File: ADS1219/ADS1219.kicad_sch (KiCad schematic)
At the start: 3 parts

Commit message: Sync
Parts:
- added C1, C2: 0.1μf, Capacitor_SMD:C_0805_2012Metric_Pad1.18x1.45mm_HandSolder, symbol Device:C
- added JP1, JP2, JP3, JP4, JP5, JP6, JP7, JP8: SolderJumper_2_Open, Jumper:SolderJumper-2_P1.3mm_Open_TrianglePad1.0x1.5mm, symbol Jumper:SolderJumper_2_Open
- added R1, R2, R3: 4.7k, Resistor_SMD:R_0805_2012Metric_Pad1.20x1.40mm_HandSolder, symbol Device:R
- J1: renamed from J?; footprint Connector_PinHeader_1.00mm:PinHeader_1x04_P1.00mm_Vertical -> Connector_JST:JST_SH_BM04B-SRSS-TB_1x04-1MP_P1.00mm_Vertical
- J2: renamed from J?; footprint Connector_PinHeader_1.00mm:PinHeader_1x06_P1.00mm_Vertical -> Connector_PinHeader_2.54mm:PinHeader_1x06_P2.54mm_Vertical
- gave numbers to parts that had none: 1
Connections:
- net +3V3: now also U1.12 (AVDD), U1.13 (DVDD), U1.3 (RESET_N), C1.2, C2.1, JP2.2 (B), JP6.2 (B), R1.1, R2.1, R3.1
- net AIN0: now also U1.11 (AIN0)
- net AIN1: now also U1.10 (AIN1)
- net AIN2: now also U1.7 (AIN2)
- net AIN3: now also U1.6 (AIN3)
- net GND: now also U1.4 (DGND), U1.5 (AVSS), C1.1, C2.2, JP1.2 (B), JP5.2 (B)
- net SCL: now also U1.16 (SCL), JP4.2 (B), JP8.2 (B), R3.2
- net SDA: now also U1.15 (SDA), JP3.2 (B), JP7.2 (B), R1.2
- net A0: now reaches U1.1 (A0)
- net A0: now also JP5.1 (A), JP6.1 (A), JP7.1 (A), JP8.1 (A)
- net at U1.14 (DRDY_N): now also R2.2
- net A1: now reaches U1.2 (A1)
- net A1: now also JP1.1 (A), JP2.1 (A), JP3.1 (A), JP4.1 (A)
- no-connect marks 0 -> 2

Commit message: futher revisions
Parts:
- added H1, H2: MountingHole, MountingHole:MountingHole_2.5mm, symbol Mechanical:MountingHole
- J1: footprint Connector_JST:JST_SH_BM04B-SRSS-TB_1x04-1MP_P1.00mm_Vertical -> Connector_JST:JST_SH_SM04B-SRSS-TB_1x04-1MP_P1.00mm_Horizontal
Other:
- company: (none) -> BecauseImclever.com
- moved on the sheet: C1, C2, J1, J2, JP1, JP2, JP3, JP4, JP5, JP6, JP7, JP8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

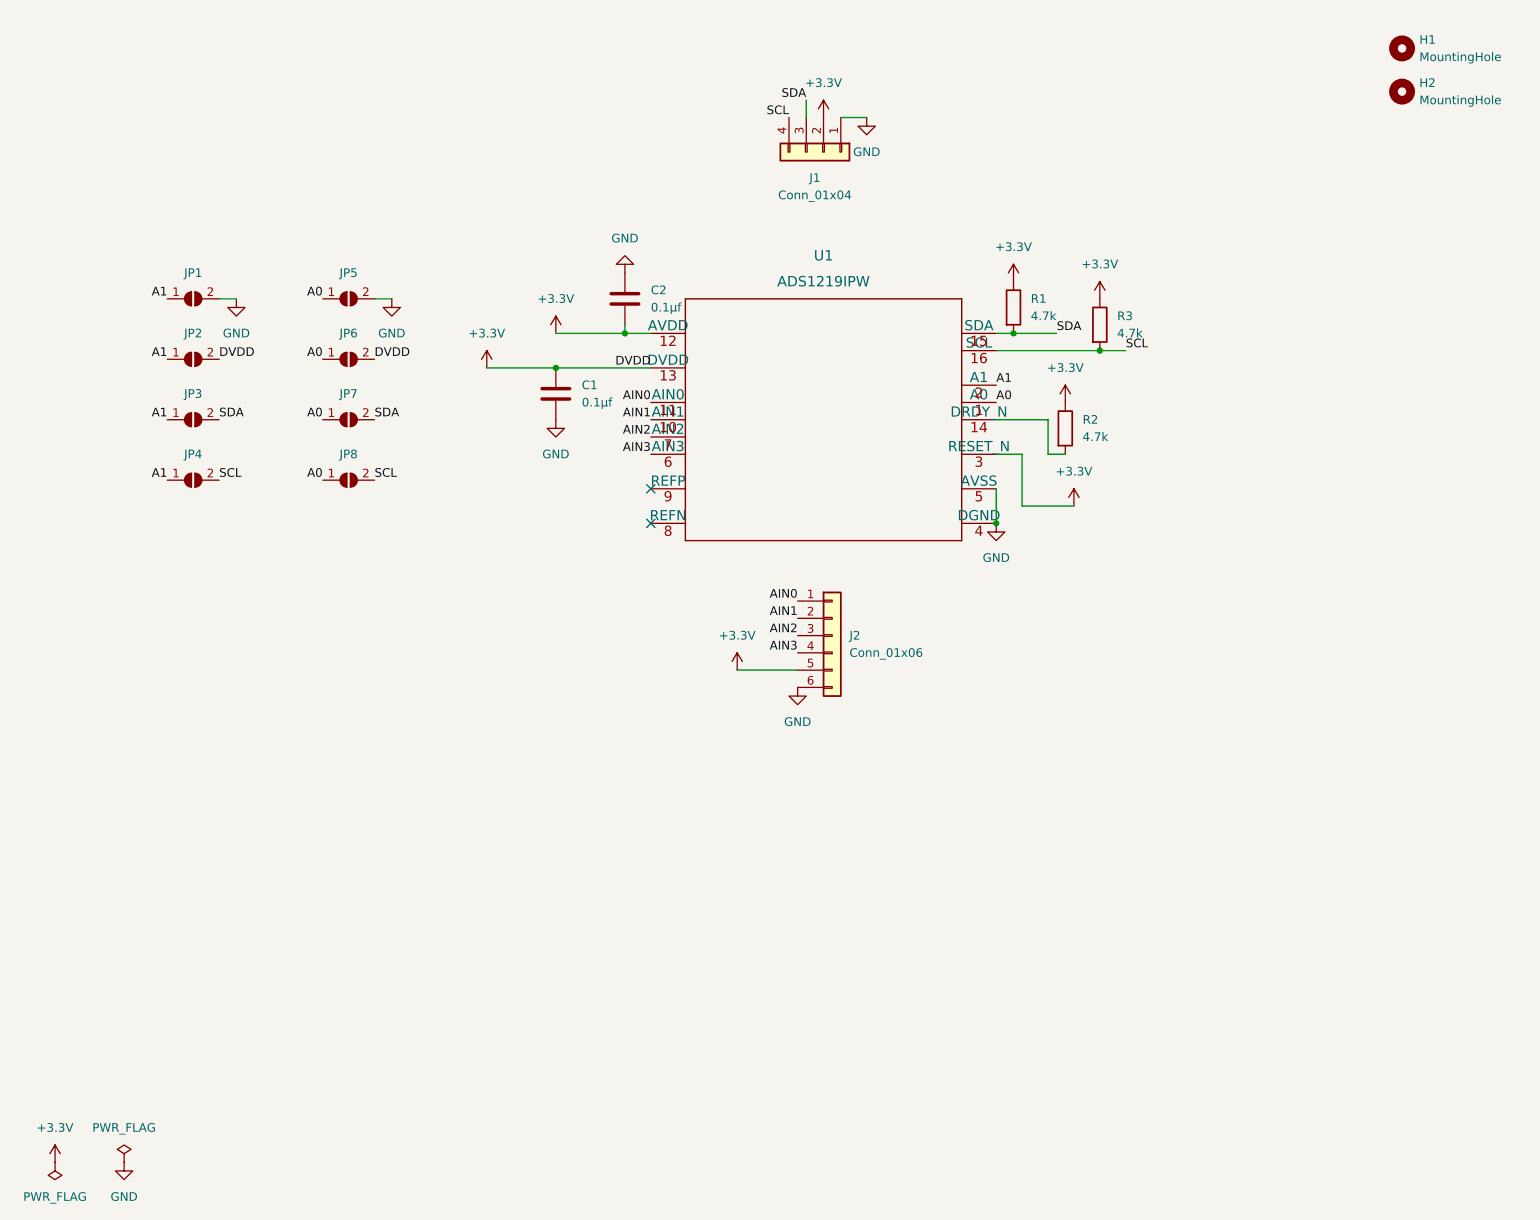
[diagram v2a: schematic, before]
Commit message: ADC nearly complete
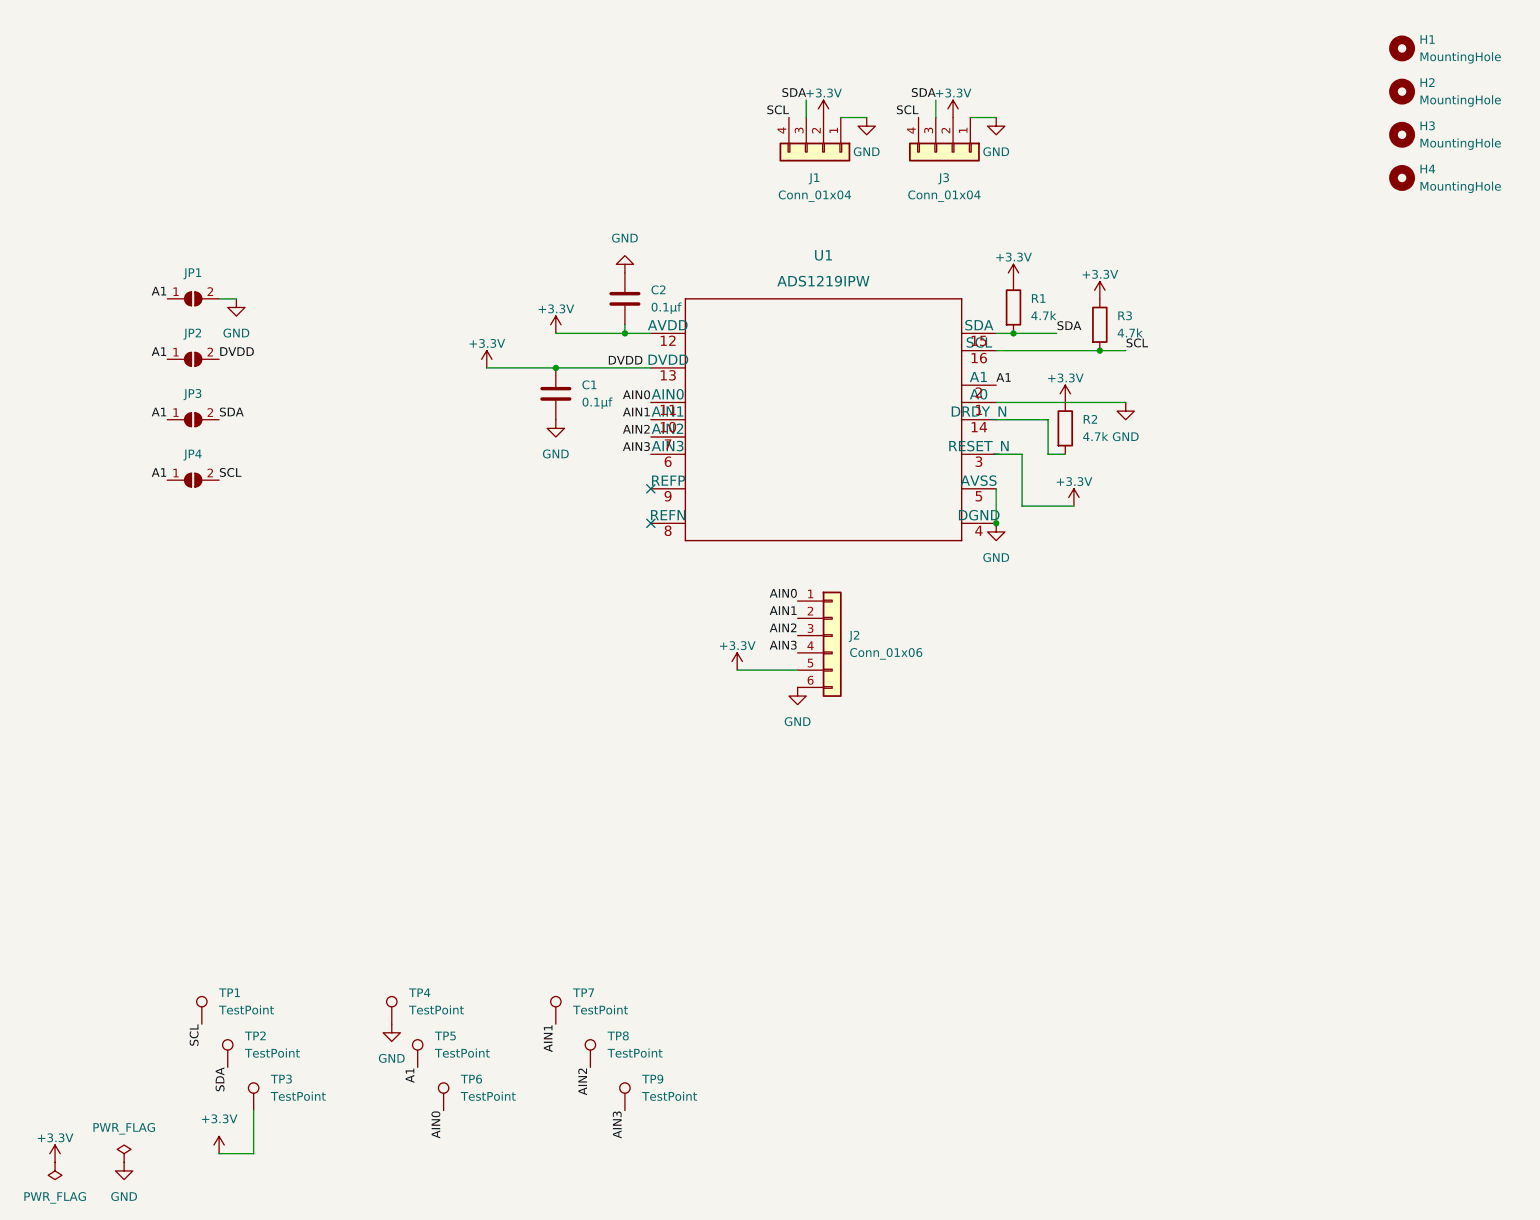
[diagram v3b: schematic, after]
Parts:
- removed JP5, JP6, JP7, JP8: SolderJumper_2_Open, Jumper:SolderJumper-2_P1.3mm_Open_TrianglePad1.0x1.5mm, symbol Jumper:SolderJumper_2_Open
- added H3, H4: MountingHole, MountingHole:MountingHole_2.5mm, symbol Mechanical:MountingHole
- added J3: Conn_01x04, Connector_JST:JST_SH_SM04B-SRSS-TB_1x04-1MP_P1.00mm_Horizontal, symbol Connector_Generic:Conn_01x04
- added TP1, TP2, TP3, TP4, TP5, TP6, TP7, TP8, TP9: TestPoint, TestPoint:TestPoint_Pad_1.0x1.0mm, symbol Connector:TestPoint
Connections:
- net A0 is gone; now on net GND: U1.1 (A0)
- net A1: now also TP5.1
- net AIN0: now also TP6.1
- net AIN1: now also TP7.1
- net AIN2: now also TP8.1
- net AIN3: now also TP9.1
- net GND: now also J3.1 (Pin_1), TP4.1
- net SCL: now also J3.4 (Pin_4), TP1.1
- net SDA: now also J3.3 (Pin_3), TP2.1
- net +3V3 renamed +3.3V
- net +3.3V: now also J3.2 (Pin_2), TP3.1

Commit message: Updating the adc board with a vref
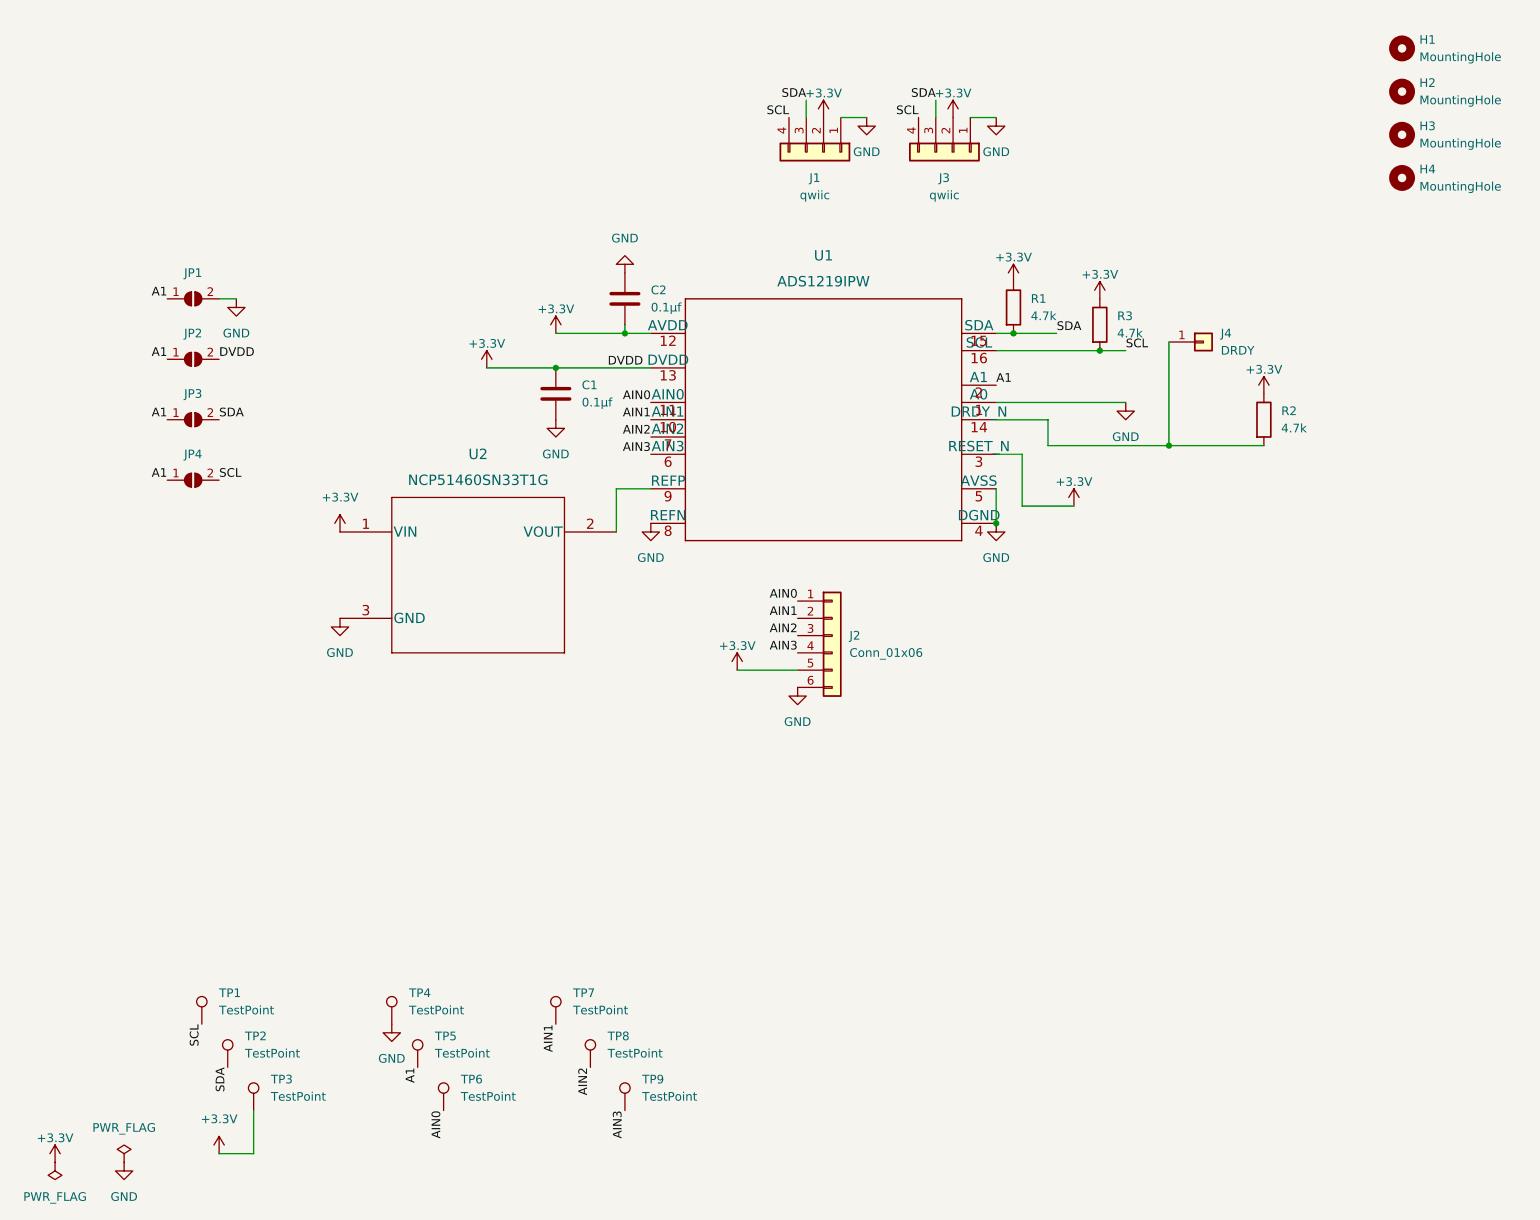
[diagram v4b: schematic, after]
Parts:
- added J4: DRDY, symbol Connector_Generic:Conn_01x01
- added U2: NCP51460SN33T1G, NCP51460SN33T1G:NCP51460SN33T1G, symbol NCP51460SN33T1G:NCP51460SN33T1G
- J1, J3: value Conn_01x04 -> qwiic
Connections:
- net +3.3V: now also U2.1 (VIN)
- net GND: now also U1.8 (REFN), U2.3 (GND)
- net at R2.2, U1.14 (DRDY_N): now also J4.1 (Pin_1)
- net at U1.9 (REFP): now also U2.2 (VOUT)
- no-connect marks 2 -> 0
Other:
- moved on the sheet: R2

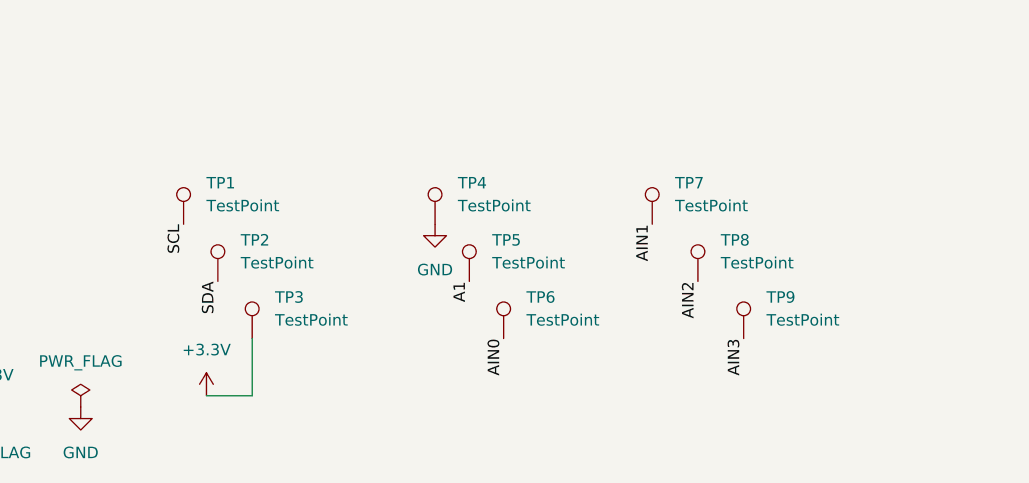
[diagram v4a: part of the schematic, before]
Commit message: Adding vref and drdy
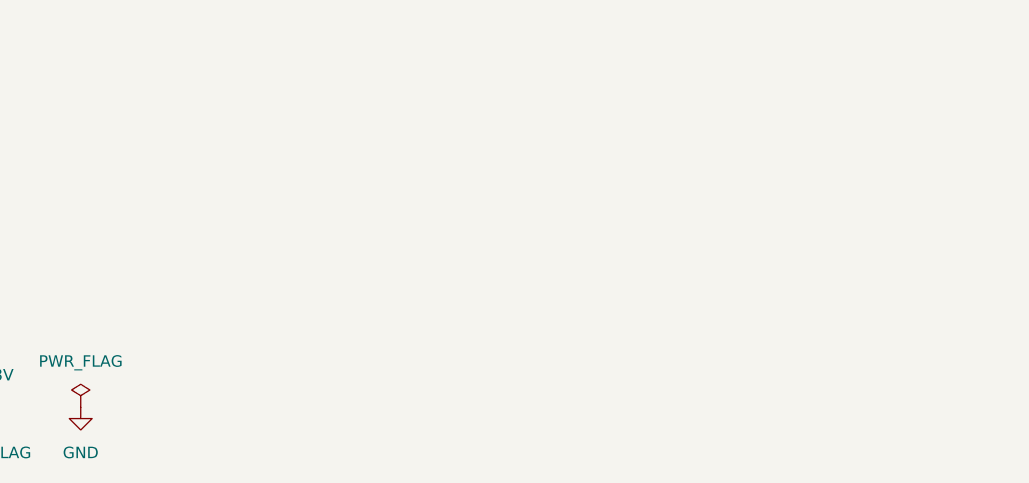
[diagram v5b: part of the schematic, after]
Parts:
- removed TP1, TP2, TP3, TP4, TP5, TP6, TP7, TP8, TP9: TestPoint, TestPoint:TestPoint_Pad_1.0x1.0mm, symbol Connector:TestPoint
- J4: footprint (none) -> Connector_PinHeader_2.54mm:PinHeader_1x01_P2.54mm_Vertical
